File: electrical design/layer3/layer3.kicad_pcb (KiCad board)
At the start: 2 copper layers, 0 parts

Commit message: almost final layer 3 pcb design
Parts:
- added BT1: Conn_01x06_Female, Connector_PinHeader_2.54mm:PinHeader_1x06_P2.54mm_Vertical, F.Cu at (68.0, 103.7)
- added BUCK1: +5V, Connector_PinHeader_2.54mm:PinHeader_1x03_P2.54mm_Vertical, F.Cu at (123.5, 153.0)
- added BUCK2: +3V3, Connector_PinHeader_2.54mm:PinHeader_1x03_P2.54mm_Vertical, F.Cu at (102.5, 153.0)
- added C1: 1μF, Capacitor_SMD:C_0603_1608Metric, B.Cu at (101.6, 92.8)
- added C10: 1μF, Capacitor_SMD:C_0603_1608Metric, B.Cu at (101.6, 121.8)
- added C11: 1pF, Capacitor_SMD:C_0603_1608Metric, B.Cu at (128.6, 116.8)
- added C12: 1pF, Capacitor_SMD:C_0603_1608Metric, B.Cu at (128.6, 120.8)
- added C2: 1μF, Capacitor_SMD:C_0603_1608Metric, B.Cu at (101.6, 94.8)
- added C3: 1μF, Capacitor_SMD:C_0603_1608Metric, B.Cu at (101.6, 96.8)
- added C4: 1μF, Capacitor_SMD:C_0603_1608Metric, B.Cu at (101.6, 98.8)
- added C5: 1pF, Capacitor_SMD:C_0603_1608Metric, B.Cu at (128.6, 93.8)
- added C6: 1pF, Capacitor_SMD:C_0603_1608Metric, B.Cu at (128.6, 97.8)
- added C7: 1μF, Capacitor_SMD:C_0603_1608Metric, B.Cu at (101.6, 115.8)
- added C8: 1μF, Capacitor_SMD:C_0603_1608Metric, B.Cu at (101.6, 117.8)
- added C9: 1μF, Capacitor_SMD:C_0603_1608Metric, B.Cu at (101.6, 119.8)
- added D1: BLUE, Diode_SMD:D_0603_1608Metric, B.Cu at (117.5, 104.8)
- added D2: BLUE, Diode_SMD:D_0603_1608Metric, B.Cu at (117.6, 127.8)
- added DRIBBLERJ1: XT30UPB-F, Connector_AMASS:AMASS_XT30UPB-F_1x02_P5.0mm_Vertical, F.Cu at (153.0, 111.5)
- added DRIBBLERJ2: Conn_01x03_Male, Connector_PinHeader_2.54mm:PinHeader_1x03_P2.54mm_Vertical, F.Cu at (84.0, 53.5)
- added J10: SH1.0 Female, Connector_JST:JST_SH_BM06B-SRSS-TB_1x06-1MP_P1.00mm_Vertical, B.Cu at (102.6, 103.8)
- added J11: SH1.0 Female, Connector_JST:JST_SH_BM06B-SRSS-TB_1x06-1MP_P1.00mm_Vertical, B.Cu at (102.6, 126.8)
- added J12: SH1.0 8P, Connector_JST:JST_SH_BM08B-SRSS-TB_1x08-1MP_P1.00mm_Vertical, F.Cu at (136.0, 62.0)
- added J13: SH1.0 8P, Connector_JST:JST_SH_BM08B-SRSS-TB_1x08-1MP_P1.00mm_Vertical, F.Cu at (149.0, 62.0)
- added J14: SH1.0 8P, Connector_JST:JST_SH_BM08B-SRSS-TB_1x08-1MP_P1.00mm_Vertical, F.Cu at (136.2, 68.2)
- added J15: SH1.0 8P, Connector_JST:JST_SH_BM08B-SRSS-TB_1x08-1MP_P1.00mm_Vertical, F.Cu at (149.0, 68.2)
- added J16: Conn_01x06_Male, Connector_JST:JST_GH_SM06B-GHS-TB_1x06-1MP_P1.25mm_Horizontal, F.Cu at (156.0, 150.0)
- added J3: XT30UPB-F, Connector_AMASS:AMASS_XT30UPB-F_1x02_P5.0mm_Vertical, F.Cu at (169.0, 103.5)
- added J4: XT30UPB-F, Connector_AMASS:AMASS_XT30UPB-F_1x02_P5.0mm_Vertical, F.Cu at (161.0, 103.5)
- added J5: XT30UPB-F, Connector_AMASS:AMASS_XT30UPB-F_1x02_P5.0mm_Vertical, F.Cu at (169.0, 111.8)
- added J6: XT30UPB-F, Connector_AMASS:AMASS_XT30UPB-F_1x02_P5.0mm_Vertical, F.Cu at (161.0, 111.5)
- added J7: XT30UPB-F, Connector_AMASS:AMASS_XT30UPB-F_1x02_P5.0mm_Vertical, F.Cu at (153.0, 103.5)
- added J8: Conn_01x06_Male, Connector_PinHeader_2.54mm:PinHeader_1x06_P2.54mm_Vertical, F.Cu at (68.0, 137.7)
- added J9: SH1.0 3P, Connector_JST:JST_SH_SM03B-SRSS-TB_1x03-1MP_P1.00mm_Horizontal, F.Cu at (76.0, 146.0)
- added LIDAR1: XH2.54 5P, Connector_JST:JST_XH_B5B-XH-AM_1x05_P2.50mm_Vertical, F.Cu at (145.0, 145.0)
- added R1: R, Resistor_SMD:R_0603_1608Metric, F.Cu at (61.0, 136.0)
- added R10: 10k, Resistor_SMD:R_0603_1608Metric, B.Cu at (118.6, 123.8)
- added R2: R, Resistor_SMD:R_0603_1608Metric, F.Cu at (61.0, 141.0)
- added R3: 10k, Resistor_SMD:R_0603_1608Metric, B.Cu at (118.6, 91.5)
- added R4: 1k, Resistor_SMD:R_0603_1608Metric, B.Cu at (113.6, 104.8)
- added R5: 1k, Resistor_SMD:R_0603_1608Metric, B.Cu at (128.6, 104.8)
- added R6: 10k, Resistor_SMD:R_0603_1608Metric, B.Cu at (118.6, 100.8)
- added R7: 10k, Resistor_SMD:R_0603_1608Metric, B.Cu at (118.6, 114.5)
- added R8: 1k, Resistor_SMD:R_0603_1608Metric, B.Cu at (113.6, 127.8)
- added R9: 1k, Resistor_SMD:R_0603_1608Metric, B.Cu at (128.6, 127.8)
- added SW1: SW_DPDT_x2, Switches:SWITCH_SPDT_PTH_11.6X4.0MM_LOCK, B.Cu at (93.4, 98.8)
- added SW2: SW_Push, Button_Switch_SMD:SW_Push_SPST_NO_Alps_SKRK, B.Cu at (123.6, 102.8)
- added SW3: SW_DPDT_x2, Switches:SWITCH_SPDT_PTH_11.6X4.0MM_LOCK, B.Cu at (93.4, 121.8)
- added SW4: SW_Push, Button_Switch_SMD:SW_Push_SPST_NO_Alps_SKRK, B.Cu at (123.6, 125.8)
- added U1: TEENSY 4.0, teensy:Teensy40, F.Cu at (110.0, 56.0)
- added U2: STM32F103C8T6, Package_QFP:LQFP-48_7x7mm_P0.5mm, B.Cu at (111.6, 95.8)
- added U3: STM32F103C8T6, Package_QFP:LQFP-48_7x7mm_P0.5mm, B.Cu at (111.6, 118.8)
- added U4: 74LVC2G04, Package_TO_SOT_SMD:SOT-23-6, F.Cu at (120.0, 69.0)
- added U5: 74LVC2G04, Package_TO_SOT_SMD:SOT-23-6, F.Cu at (125.0, 69.0)
- added Y1: Crystal, Crystal:Crystal_SMD_5032-2Pin_5.0x3.2mm, B.Cu at (123.6, 95.8)
- added Y2: Crystal, Crystal:Crystal_SMD_5032-2Pin_5.0x3.2mm, B.Cu at (123.6, 118.8)
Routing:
- net +5V: track 0.00 -> 24.8 mm
- net /M4INA: track 0.00 -> 7.65 mm
- net /M2INA: track 0.00 -> 7.62 mm
- net /M3INA: track 0.00 -> 4.47 mm
- net /M1INA: track 0.00 -> 4.44 mm
- added copper zone on F.Cu, net +12V
- added copper zone on B.Cu, net GND
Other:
- board outline added: 140 x 140 mm

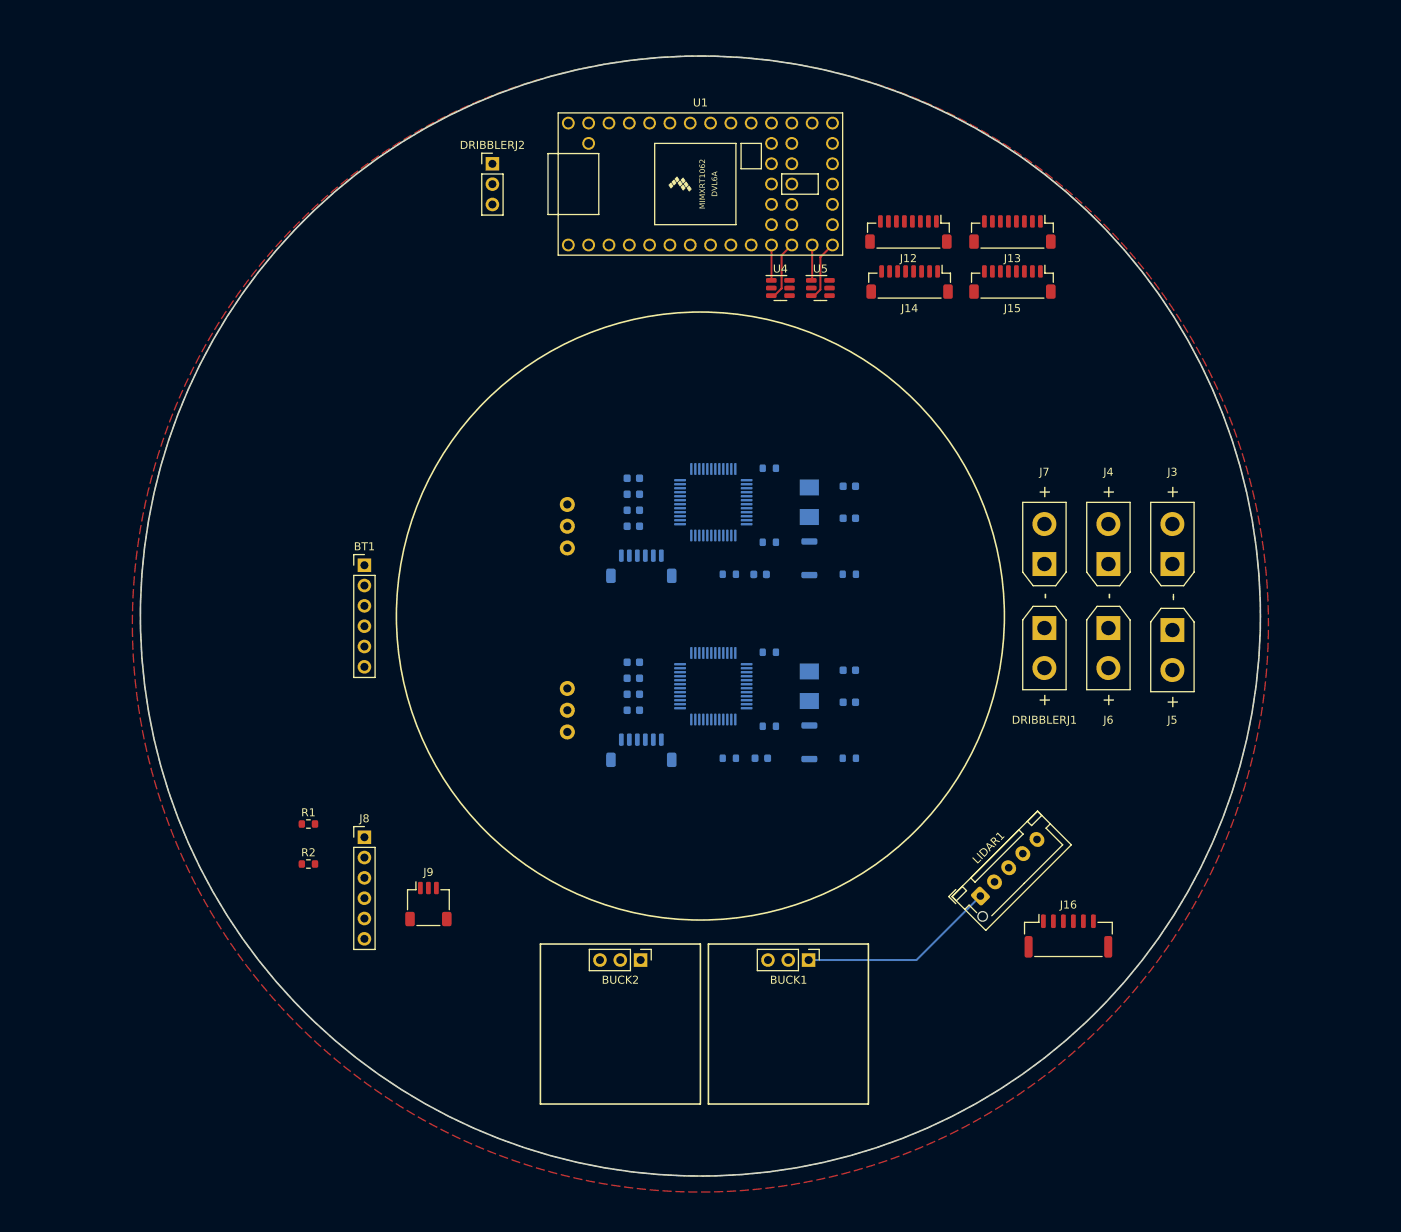
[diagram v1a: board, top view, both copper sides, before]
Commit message: update l1, l3, and driver pcbs
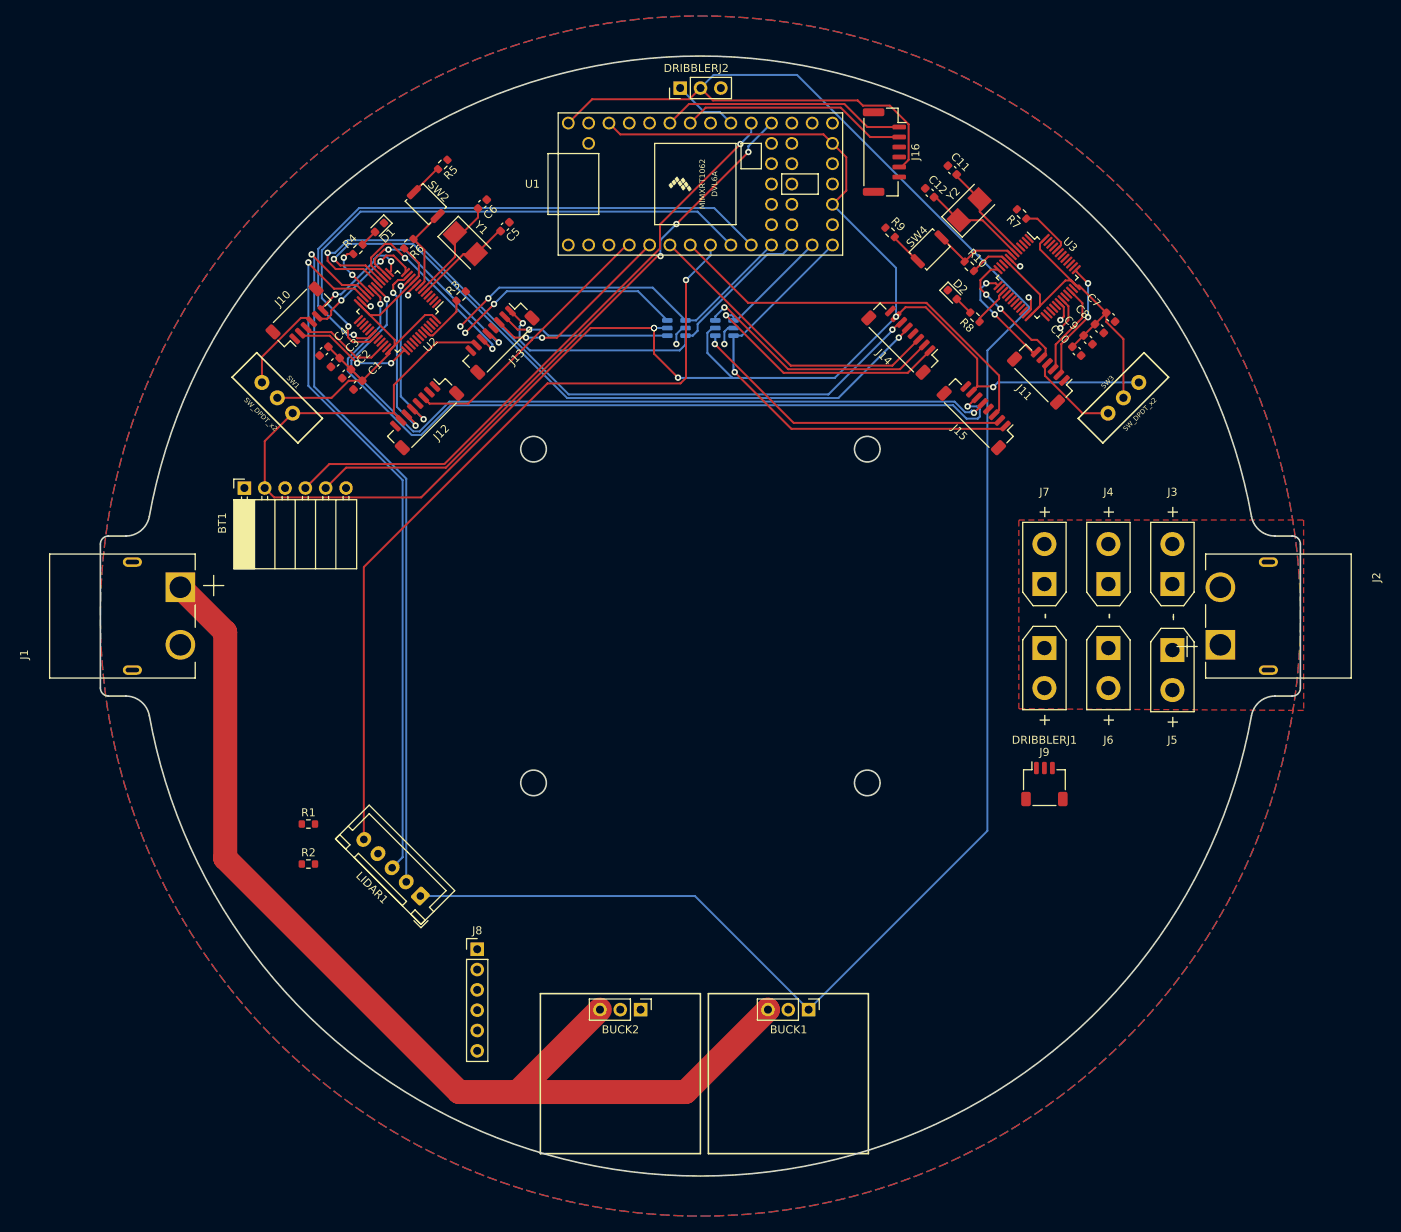
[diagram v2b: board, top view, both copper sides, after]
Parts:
- added J1: XT60PW-M, XT60PW-M:AMASS_XT60PW-M, F.Cu at (39.0, 110.0)
- added J2: XT60PW-M, XT60PW-M:AMASS_XT60PW-M, F.Cu at (181.0, 110.0)
- BT1: footprint Connector_PinHeader_2.54mm:PinHeader_1x06_P2.54mm_Vertical -> Connector_PinSocket_2.54mm:PinSocket_1x06_P2.54mm_Horizontal
- C1, C10, C11, C12, C2, C3, C4, C5, C6, C7, C8, C9, D1, D2, J10, J11, R10, R3, R4, R5, R6, R7, R8, R9, SW1, SW2, SW3, SW4, U2, U3, Y1, Y2: moved to F.Cu
- J12: value SH1.0 8P -> MOTOR1
- J13: value SH1.0 8P -> MOTOR2
- J14: value SH1.0 8P -> MOTOR3
- J15: value SH1.0 8P -> MOTOR4
- J16: value Conn_01x06_Male -> CAMERA
- J8: value Conn_01x06_Male -> COMPASS
- LIDAR1: footprint Connector_JST:JST_XH_B5B-XH-AM_1x05_P2.50mm_Vertical -> Connector_JST:JST_XH_B5B-XH-A_1x05_P2.50mm_Vertical
- U4, U5: moved to B.Cu
- moved J16 100.7 mm to (133.0, 52.0), turned to -90 degrees
- moved SW3 79.7 mm to (162.9, 82.7), turned to -45 degrees
- moved J9 78.4 mm to (153.0, 131.0)
- moved C7 73.6 mm to (161.3, 72.6), turned to 135 degrees
- moved C8 72.8 mm to (159.9, 74.1), turned to 135 degrees
- moved R5 72.2 mm to (77.8, 53.6), turned to -135 degrees
- moved C9 72.1 mm to (158.5, 75.5), turned to 135 degrees
- moved C10 71.3 mm to (157.0, 76.9), turned to 135 degrees
- moved LIDAR1 70.0 mm to (75.0, 145.0), turned to 135 degrees
- moved J11 68.8 mm to (152.8, 79.7), turned to 135 degrees
- moved R9 65.9 mm to (133.7, 62.0), turned to -45 degrees
- moved J13 65.6 mm to (84.7, 75.3), turned to -135 degrees
- moved SW2 65.3 mm to (75.7, 58.5), turned to -45 degrees
- moved U3 65.2 mm to (152.1, 67.7), turned to -45 degrees
- moved J12 64.8 mm to (75.3, 84.7), turned to -135 degrees
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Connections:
- J12 pad 1: /INA -> /M1INA
- J12 pad 2: /INB -> /M1INB
- J12 pad 3: /PWM -> /M1PWM
- J12 pad 4: /CS -> /M1CS
- J12 pad 5: /C1 -> /M1C1
- J12 pad 6: /C2 -> /M1C2
- J13 pad 1: /INA -> /M2INA
- J13 pad 2: /INB -> /M2INB
- J13 pad 3: /PWM -> /M2PWM
- J13 pad 4: /CS -> /M2CS
- J13 pad 5: /C1 -> /M2C1
- J13 pad 6: /C2 -> /M2C2
- J14 pad 1: /INA -> /M3INA
- J14 pad 2: /INB -> /M3INB
- J14 pad 3: /PWM -> /M3PWM
- J14 pad 4: /CS -> /M3CS
- J14 pad 5: /C1 -> /M3C1
- J14 pad 6: /C2 -> /M3C2
- J15 pad 1: /INA -> /M4INA
- J15 pad 2: /INB -> /M4INB
- J15 pad 3: /PWM -> /M4PWM
- J15 pad 4: /CS -> /M4CS
- J15 pad 5: /C1 -> /M4C1
- J15 pad 6: /C2 -> /M4C2
- J7 pad 2: /BATT_+12V -> +12V
- LIDAR1 pad 5: /MOTOCT -> /LIDARPWM
- U1 pad 6: /DRIBBLERPWM -> /LIDARPWM
- U2 pad 10: unconnected-(U2-Pad10) -> /M1C1
- U2 pad 11: unconnected-(U2-Pad11) -> /M1C2
- U2 pad 12: unconnected-(U2-Pad12) -> /DEBUGTX1
- U2 pad 14: /DEBUGTX1 -> /M2C1
- U2 pad 15: Net-(R4-Pad1) -> /M2C2
- U2 pad 16: unconnected-(U2-Pad16) -> /M3C1
- U2 pad 17: unconnected-(U2-Pad17) -> /M3C2
- U2 pad 18: unconnected-(U2-Pad18) -> /M4C1
- U2 pad 19: unconnected-(U2-Pad19) -> /M4C2
- U2 pad 20: unconnected-(U2-Pad20) -> Net-(R4-Pad1)
- U2 pad 21: unconnected-(U2-Pad21) -> /LIDARTX
- U2 pad 22: unconnected-(U2-Pad22) -> /LIDARRX
- U3 pad 12: unconnected-(U3-Pad12) -> /DEBUGTX2
- U3 pad 14: /DEBUGTX2 -> unconnected-(U3-Pad14)
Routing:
- net +3V3: track 0.00 -> 240.3 mm, vias 0 -> 5
- net +5V: track 24.8 -> 259.7 mm
- net /BATT_+12V: track 0.00 -> 135.0 mm
- net /LIDARPWM: track 0.00 -> 102.0 mm, vias 0 -> 1
- net /M4C2: track 0.00 -> 101.2 mm, vias 0 -> 2
- net /M4C1: track 0.00 -> 97.8 mm, vias 0 -> 2
- net /M3C2: track 0.00 -> 92.7 mm, vias 0 -> 2
- net /LIDARTX: track 0.00 -> 92.3 mm, vias 0 -> 1
- net /M3C1: track 0.00 -> 91.2 mm, vias 0 -> 2
- net /LIDARRX: track 0.00 -> 89.9 mm, vias 0 -> 1
- net /BTTX: track 0.00 -> 77.1 mm, vias 0 -> 1
- net /BTRX: track 0.00 -> 76.3 mm, vias 0 -> 3
- net /L4TX: track 0.00 -> 74.0 mm, vias 0 -> 1
- net /L4RX: track 0.00 -> 71.1 mm, vias 0 -> 1
- net /MCU3V31: track 0.00 -> 53.1 mm
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- added copper zone on F.Cu, net GND
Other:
- board size 140 x 140 mm -> 150 x 140 mm

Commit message: almost final pcbs
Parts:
- added J17: SH1.0 3P, Connector_JST:JST_SH_BM03B-SRSS-TB_1x03-1MP_P1.00mm_Vertical, F.Cu at (148.0, 157.0)
- J9: value SH1.0 3P -> SH1.0 5P; footprint Connector_JST:JST_SH_SM03B-SRSS-TB_1x03-1MP_P1.00mm_Horizontal -> Connector_JST:JST_SH_BM05B-SRSS-TB_1x05-1MP_P1.00mm_Vertical
- moved J9 104.4 mm to (86.0, 51.0), turned to 90 degrees
- moved J2 28.4 mm to (161.9, 131.0)
- moved R1 27.8 mm to (82.8, 153.2)
- moved R2 27.3 mm to (82.8, 157.5)
- moved J8 4.44 mm to (82.7, 147.3), turned to -45 degrees
- moved BT1 2.57 mm to (55.5, 93.7)
- moved DRIBBLERJ1 1.00 mm to (154.0, 114.0)
- moved J7 1.00 mm to (154.0, 106.0)
- moved J3 1.00 mm to (170.0, 106.0)
- moved J4 1.00 mm to (162.0, 106.0)
- moved J5 1.00 mm to (170.0, 114.2)
- moved J6 1.00 mm to (162.0, 114.0)
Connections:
- J8 pad 1: /MCU3V3 -> /MCU3V32
- J9 pad 1: unconnected-(J9-Pad1) -> /L1RX
- J9 pad 2: unconnected-(J9-Pad2) -> /L1TX
- J9 pad 3: unconnected-(J9-Pad3) -> +5V
- R1 pad 2: /MCU3V3 -> /MCU3V32
- R2 pad 2: /MCU3V3 -> /MCU3V32
- U2 pad 39: unconnected-(U2-Pad39) -> /NEOPIXELOUT
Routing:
- net /IMUSDA: track 0.00 -> 160.1 mm, vias 0 -> 2
- net /IMUSCL: track 0.00 -> 150.1 mm, vias 0 -> 2
- net /IMURST: track 0.00 -> 141.2 mm, vias 0 -> 4
- net /NEOPIXELOUT: track 0.00 -> 123.0 mm, vias 0 -> 4
- net /MCU3V32: track 53.0 -> 172.3 mm, vias 0 -> 2
- net /IMURX: track 4.29 -> 55.4 mm, vias 1 -> 3
- net /IMUTX: track 2.59 -> 52.8 mm, vias 1 -> 3
- net +5V: track 259.7 -> 296.0 mm
- net /L1TX: track 0.00 -> 16.5 mm
- net /L1RX: track 0.00 -> 14.2 mm
- net +3V3: track 240.3 -> 251.6 mm, vias 5 -> 6
- net /M1INB: track 28.9 -> 38.9 mm, vias 2 -> 3
- net /M1INA: track 46.5 -> 56.0 mm, vias 2 -> 3
- net /BTTX: track 77.1 -> 74.5 mm
- net /BTRX: track 76.3 -> 73.6 mm
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- removed copper zone on F.Cu, net +12V

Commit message: submit all pcbs for production
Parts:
- added J18: XT30UPB-F, Connector_AMASS:AMASS_XT30UPB-F_1x02_P5.0mm_Vertical, F.Cu at (44.2, 122.0)
- added J19: Conn_01x01_Female, Connector_Wire:SolderWire-1.5sqmm_1x01_D1.7mm_OD3.9mm, F.Cu at (49.0, 99.0)
- added J20: Conn_01x01_Female, Connector_Wire:SolderWire-1.5sqmm_1x01_D1.7mm_OD3.9mm, F.Cu at (156.0, 142.0)
- moved J7 107.8 mm to (50.0, 134.5)
- moved SW1 7.19 mm to (62.0, 88.0), turned to -90 degrees
- moved SW3 7.18 mm to (158.0, 88.0), turned to -90 degrees
- moved J1 4.00 mm to (43.0, 110.0)
- moved J8 3.89 mm to (85.5, 144.5)
- moved J17 3.50 mm to (148.0, 153.5)
- moved R1 3.39 mm to (85.2, 150.9)
- moved R2 3.39 mm to (85.2, 155.1)
- moved DRIBBLERJ1 0.50 mm to (154.0, 113.5)
- moved J2 0.50 mm to (161.9, 130.5)
- moved J3 0.50 mm to (170.0, 105.5)
- moved J4 0.50 mm to (162.0, 105.5)
- moved J5 0.50 mm to (170.0, 113.8)
- moved J6 0.50 mm to (162.0, 113.5)
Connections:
- J2 pad 1: +12V -> /BATT_+12V
- J2 pad 2: /BATT_+12V -> +12V
- J7 pad 2: +12V -> /BATT_+12V
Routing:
- net +3V3: track 251.6 -> 363.7 mm
- net /BATT_+12V: track 135.0 -> 118.5 mm
- net GND: track 13.1 -> 5.57 mm, vias 13 -> 19
- net /PROG3V31: track 11.6 -> 18.2 mm
- net +5V: track 296.0 -> 301.0 mm
- net /IMURST: track 141.2 -> 137.3 mm
- net /MCU3V32: track 172.3 -> 168.6 mm
- net /NEOPIXELOUT: track 123.0 -> 120.4 mm
- net /IMUSCL: track 150.1 -> 152.2 mm
- net /IMUSDA: track 160.1 -> 161.2 mm
- net /SWDCLOCK1: track 15.3 -> 16.3 mm
- net /PROG3V32: track 11.5 -> 10.6 mm
- net Net-(R3-Pad1): track 6.89 -> 7.64 mm
- net /MCU3V31: track 53.1 -> 52.3 mm
- net Net-(R7-Pad1): track 6.74 -> 7.45 mm
- added copper zone on F.Cu, net +12V
- added copper zone on F.Cu, net /BATT_+12V
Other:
- board size 150 x 140 mm -> 140 x 140 mm
